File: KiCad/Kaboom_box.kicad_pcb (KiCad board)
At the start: 2 copper layers, 351.5 x 141.5 mm, 206 parts, among them J101 2mm_clamp, J102 2mm_clamp, J103 2mm_clamp, J104 2mm_clamp, J105 2mm_clamp, J106 2mm_clamp, J107 2mm_clamp, J108 2mm_clamp, J109 2mm_clamp, J110 2mm_clamp, J111 2mm_clamp, J112 2mm_clamp, J113 2mm_clamp, J114 2mm_clamp, J115 2mm_clamp, J116 2mm_clamp, J117 2mm_clamp, J118 2mm_clamp, J119 2mm_clamp, J120 2mm_clamp, J121 2mm_clamp, J122 2mm_clamp, J123 2mm_clamp, J124 2mm_clamp, J125 2mm_clamp, J126 2mm_clamp, J127 2mm_clamp, J128 2mm_clamp, J129 2mm_clamp, J130 2mm_clamp, J131 2mm_clamp, J132 2mm_clamp, J133 2mm_clamp, J134 2mm_clamp, J135 2mm_clamp, J136 2mm_clamp, J137 2mm_clamp, J138 2mm_clamp, J139 2mm_clamp, J140 2mm_clamp, J141 2mm_clamp, J142 2mm_clamp, J143 2mm_clamp, J144 2mm_clamp, J145 2mm_clamp, J146 2mm_clamp, J147 2mm_clamp, J148 2mm_clamp, J149 2mm_clamp, J150 2mm_clamp, J151 2mm_clamp, J152 2mm_clamp, J153 2mm_clamp, J154 2mm_clamp, J155 2mm_clamp, J156 2mm_clamp, J157 2mm_clamp, J158 2mm_clamp, J159 2mm_clamp, J160 2mm_clamp, J161 2mm_clamp, J162 Screw_Terminal_01x02, P101 HDR-IDC-2_54-2X5P, P102 HDR-IDC-2_54-2X5P, P103 HDR-IDC-2_54-2X5P, P104 HDR-IDC-2_54-2X5P, P105 HDR-IDC-2_54-2X5P, P106 HDR-IDC-2_54-2X5P, U101 SS54_C22452, U102 EC12E1220813, U103 RaspberryPi_Pico, U104 TS-1187A-B-A-B, U105 TS-1187A-B-A-B, U106 AO3400A, U107 WS2812E-MINI-X1, U108 WS2812E-MINI-X1, U109 WS2812E-MINI-X1, U110 WS2812E-MINI-X1, U111 WS2812E-MINI-X1, U112 WS2812E-MINI-X1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

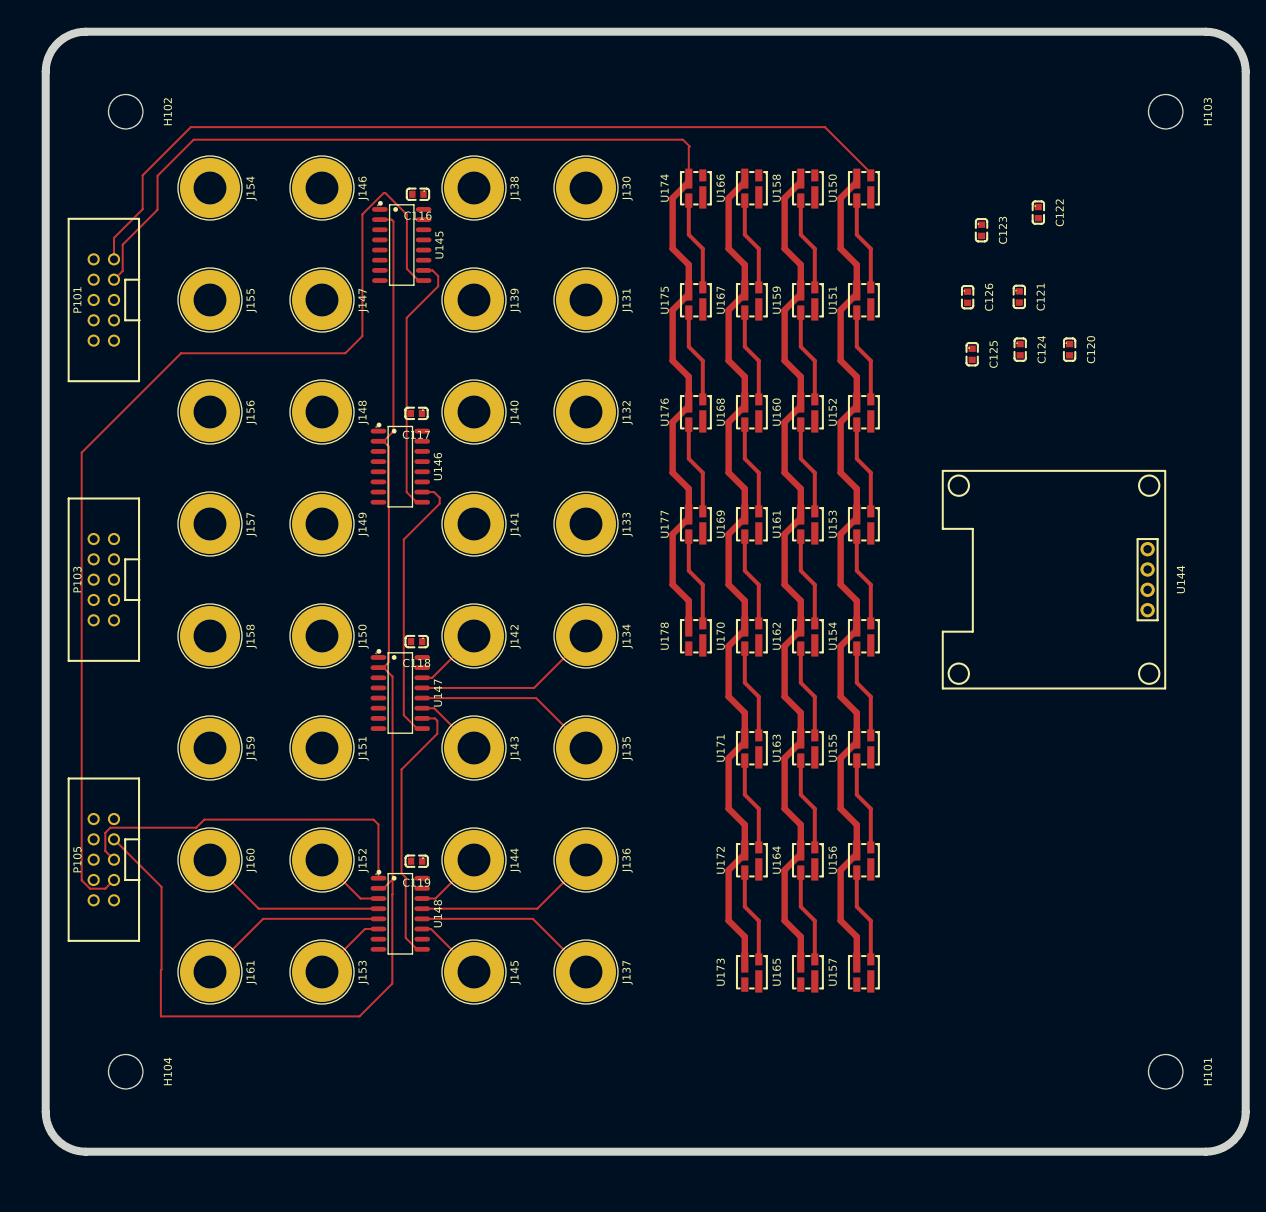
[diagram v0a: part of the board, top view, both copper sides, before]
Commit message: Update to TOP pcb - 2mm holes placement and routing
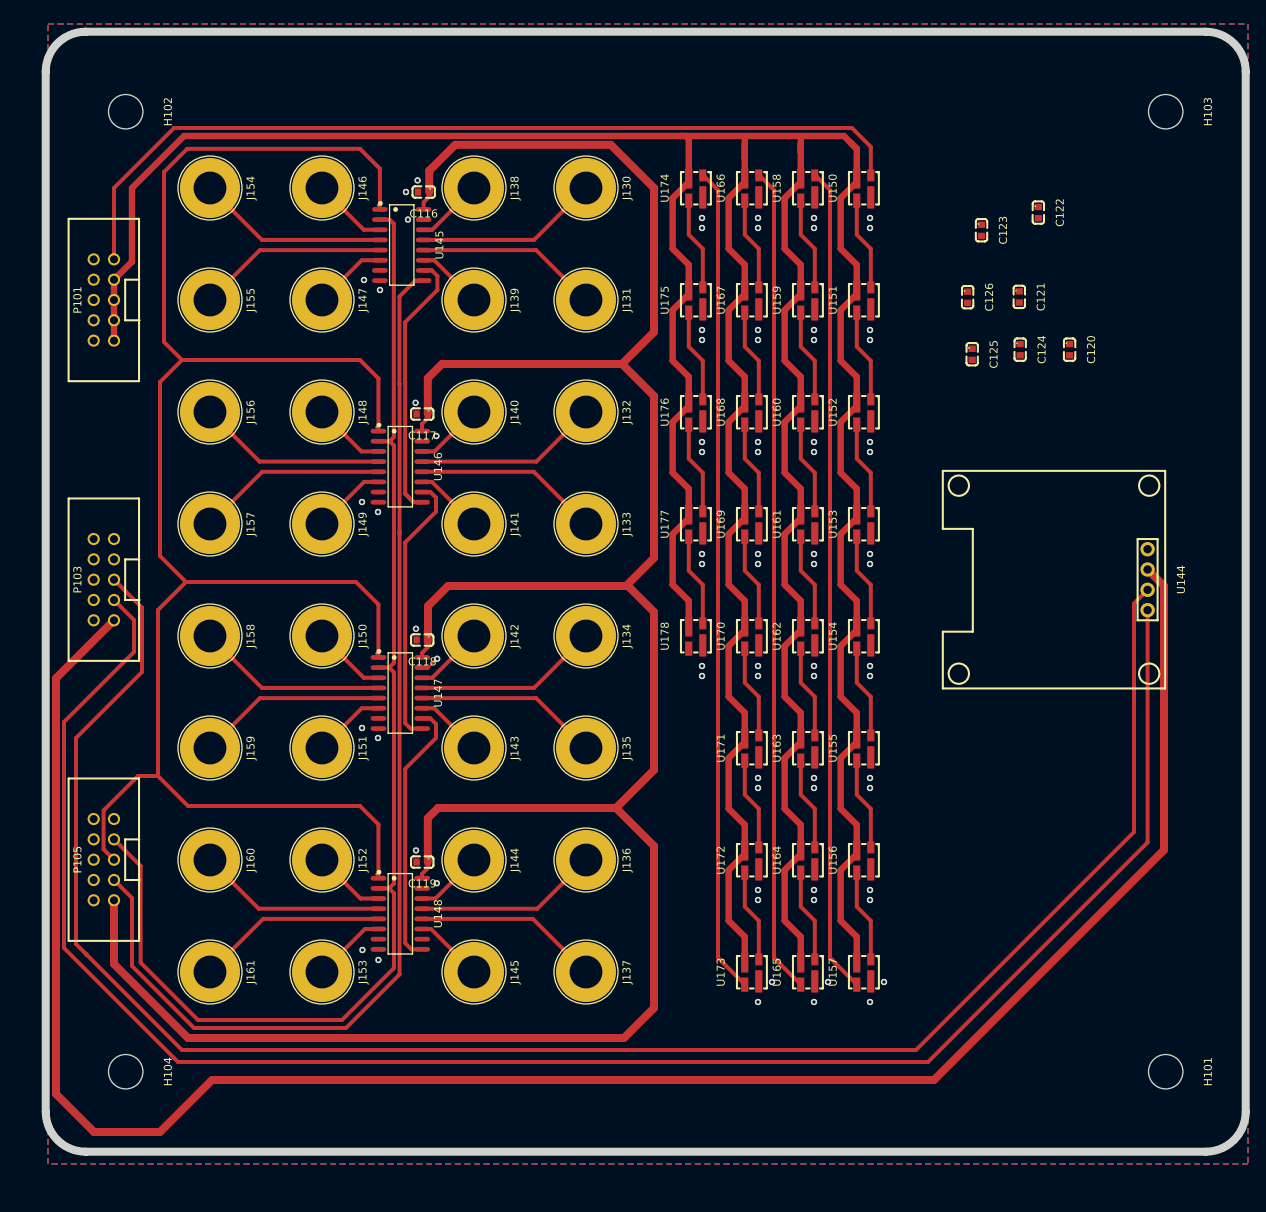
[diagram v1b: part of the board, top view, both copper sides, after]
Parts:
- moved C116 0.77 mm to (298.7, 81.5)
- moved C117 0.73 mm to (298.5, 109.2)
- moved C118 0.72 mm to (298.5, 137.5)
- moved C119 0.70 mm to (298.5, 165.2)
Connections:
- net Net-(J134-Pin_1) renamed /Top/Shift_Parallel_to_Serial/J134
- net Net-(J135-Pin_1) renamed /Top/Shift_Parallel_to_Serial/J135
- net Net-(J136-Pin_1) renamed /Top/Shift_Parallel_to_Serial/J136
- net Net-(J137-Pin_1) renamed /Top/Shift_Parallel_to_Serial/J137
- net Net-(J142-Pin_1) renamed /Top/Shift_Parallel_to_Serial/J142
- net Net-(J143-Pin_1) renamed /Top/Shift_Parallel_to_Serial/J143
- net Net-(J144-Pin_1) renamed /Top/Shift_Parallel_to_Serial/J144
- net Net-(J145-Pin_1) renamed /Top/Shift_Parallel_to_Serial/J145
- net Net-(J152-Pin_1) renamed /Top/Shift_Parallel_to_Serial/J152
- net Net-(J153-Pin_1) renamed /Top/Shift_Parallel_to_Serial/J153
- net Net-(J160-Pin_1) renamed /Top/Shift_Parallel_to_Serial/J160
- net Net-(J161-Pin_1) renamed /Top/Shift_Parallel_to_Serial/J161
- J130 pad 1: Net-(J130-Pin_1) -> /Top/Shift_Parallel_to_Serial/J130
- J131 pad 1: Net-(J131-Pin_1) -> /Top/Shift_Parallel_to_Serial/J131
- J132 pad 1: Net-(J132-Pin_1) -> /Top/Shift_Parallel_to_Serial/J132
- J133 pad 1: Net-(J133-Pin_1) -> /Top/Shift_Parallel_to_Serial/J133
- J138 pad 1: Net-(J138-Pin_1) -> /Top/Shift_Parallel_to_Serial/J138
- J139 pad 1: Net-(J139-Pin_1) -> /Top/Shift_Parallel_to_Serial/J139
- J140 pad 1: Net-(J140-Pin_1) -> /Top/Shift_Parallel_to_Serial/J140
- J141 pad 1: Net-(J141-Pin_1) -> /Top/Shift_Parallel_to_Serial/J141
- J146 pad 1: unconnected-(J146-Pin_1-Pad1) -> /Top/Shift_Parallel_to_Serial/J146
- J147 pad 1: unconnected-(J147-Pin_1-Pad1) -> /Top/Shift_Parallel_to_Serial/J147
- J148 pad 1: unconnected-(J148-Pin_1-Pad1) -> /Top/Shift_Parallel_to_Serial/J148
- J149 pad 1: unconnected-(J149-Pin_1-Pad1) -> /Top/Shift_Parallel_to_Serial/J149
- J150 pad 1: unconnected-(J150-Pin_1-Pad1) -> /Top/Shift_Parallel_to_Serial/J150
- J151 pad 1: unconnected-(J151-Pin_1-Pad1) -> /Top/Shift_Parallel_to_Serial/J151
- J154 pad 1: unconnected-(J154-Pin_1-Pad1) -> /Top/Shift_Parallel_to_Serial/J154
- J155 pad 1: unconnected-(J155-Pin_1-Pad1) -> /Top/Shift_Parallel_to_Serial/J155
- J156 pad 1: unconnected-(J156-Pin_1-Pad1) -> /Top/Shift_Parallel_to_Serial/J156
- J157 pad 1: unconnected-(J157-Pin_1-Pad1) -> /Top/Shift_Parallel_to_Serial/J157
- J158 pad 1: unconnected-(J158-Pin_1-Pad1) -> /Top/Shift_Parallel_to_Serial/J158
- J159 pad 1: unconnected-(J159-Pin_1-Pad1) -> /Top/Shift_Parallel_to_Serial/J159
- U145 pad 11: unconnected-(U145-D0-Pad11) -> /Top/Shift_Parallel_to_Serial/J139
- U145 pad 12: Net-(J139-Pin_1) -> /Top/Shift_Parallel_to_Serial/J131
- U145 pad 13: unconnected-(U145-D2-Pad13) -> /Top/Shift_Parallel_to_Serial/J130
- U145 pad 14: Net-(J131-Pin_1) -> /Top/Shift_Parallel_to_Serial/J138
- U145 pad 3: Net-(J130-Pin_1) -> /Top/Shift_Parallel_to_Serial/J146
- U145 pad 4: unconnected-(U145-D5-Pad4) -> /Top/Shift_Parallel_to_Serial/J154
- U145 pad 5: Net-(J138-Pin_1) -> /Top/Shift_Parallel_to_Serial/J155
- U145 pad 6: unconnected-(U145-D7-Pad6) -> /Top/Shift_Parallel_to_Serial/J147
- U146 pad 11: unconnected-(U146-D0-Pad11) -> /Top/Shift_Parallel_to_Serial/J141
- U146 pad 12: Net-(J141-Pin_1) -> /Top/Shift_Parallel_to_Serial/J133
- U146 pad 13: unconnected-(U146-D2-Pad13) -> /Top/Shift_Parallel_to_Serial/J132
- U146 pad 14: Net-(J133-Pin_1) -> /Top/Shift_Parallel_to_Serial/J140
- U146 pad 3: Net-(J132-Pin_1) -> /Top/Shift_Parallel_to_Serial/J148
- U146 pad 4: unconnected-(U146-D5-Pad4) -> /Top/Shift_Parallel_to_Serial/J156
- U146 pad 5: Net-(J140-Pin_1) -> /Top/Shift_Parallel_to_Serial/J157
- U146 pad 6: unconnected-(U146-D7-Pad6) -> /Top/Shift_Parallel_to_Serial/J149
- U147 pad 3: unconnected-(U147-D4-Pad3) -> /Top/Shift_Parallel_to_Serial/J150
- U147 pad 4: unconnected-(U147-D5-Pad4) -> /Top/Shift_Parallel_to_Serial/J158
- U147 pad 5: unconnected-(U147-D6-Pad5) -> /Top/Shift_Parallel_to_Serial/J159
- U147 pad 6: unconnected-(U147-D7-Pad6) -> /Top/Shift_Parallel_to_Serial/J151
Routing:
- net /Top/+3.3V: track 0.00 -> 580.2 mm
- net /I2C_SCL_LID: track 0.00 -> 230.8 mm
- net /I2C1_SDA_LID: track 0.00 -> 229.9 mm
- net /SPI0_CSn_LID: track 45.6 -> 230.7 mm
- net Net-(U173-DO): track 0.00 -> 103.4 mm
- net Net-(U165-DO): track 0.00 -> 103.4 mm
- net Net-(U157-DO): track 0.00 -> 103.4 mm
- net /Top/VDD: track 498.9 -> 549.7 mm
- net /Top/Shift_Parallel_to_Serial/J154: track 0.00 -> 23.9 mm
- net /Top/Shift_Parallel_to_Serial/J155: track 0.00 -> 23.8 mm
- net /Top/Shift_Parallel_to_Serial/J157: track 0.00 -> 23.8 mm
- net /Top/Shift_Parallel_to_Serial/J158: track 0.00 -> 23.7 mm
- net /Top/Shift_Parallel_to_Serial/J159: track 0.00 -> 23.6 mm
- net /Top/Shift_Parallel_to_Serial/J156: track 0.00 -> 23.6 mm
- net /Top/Shift_Parallel_to_Serial/J133: track 0.00 -> 23.2 mm
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- added copper zone on B.Cu, net /Top/GND
- added copper zone on F.Cu, net /Top/GND

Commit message: WIP on Bottom
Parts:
- moved R104 18.9 mm to (98.5, 181.2)
- moved R103 4.41 mm to (105.8, 182.3)
- moved R111 3.43 mm to (98.5, 153.2), turned to 180 degrees
- moved R110 3.15 mm to (98.5, 155.7), turned to 180 degrees
- moved R102 3.03 mm to (105.8, 179.8)
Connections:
- U103 pad 16: unconnected-(U103-GPIO12-Pad16) -> /Bottom/+3.3V
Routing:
- net /Bottom/VDD: track 525.4 -> 870.2 mm
- net /I2C_SCL_BOT: track 4.90 -> 265.3 mm, vias 0 -> 2
- net /I2C1_SDA_BOT: track 4.89 -> 261.9 mm, vias 0 -> 2
- net /Bottom/LED_DATA_OUT: track 0.00 -> 254.9 mm
- net /Bottom/+3.3V: track 270.2 -> 443.5 mm
- net Net-(J101-Pin_1): track 0.00 -> 117.4 mm
- net Net-(U130-DO): track 0.00 -> 103.3 mm
- net Net-(U122-DO): track 0.00 -> 103.3 mm
- net Net-(U114-DO): track 0.00 -> 103.3 mm
- net Net-(J104-Pin_1): track 0.00 -> 96.8 mm
- net /Bottom/SPI1_CSn: track 49.9 -> 142.2 mm, vias 3 -> 11
- net /Bottom/SPI1_RST: track 48.9 -> 140.8 mm, vias 4 -> 6
- net Net-(J107-Pin_1): track 0.00 -> 82.7 mm
- net /Bottom/SPI1_TX: track 67.7 -> 143.8 mm
- net /Bottom/SPI1_SCK: track 84.8 -> 157.7 mm
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
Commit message: Layout wip
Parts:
- J162: moved to B.Cu
- moved D102 44.1 mm to (137.2, 174.7)
- moved U149 40.6 mm to (138.8, 181.6), turned to 180 degrees
- moved R120 40.1 mm to (134.8, 181.7), turned to -90 degrees
- moved J162 39.5 mm to (139.9, 177.7), turned to 180 degrees
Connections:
- net /Bottom/SPI1_RST renamed /Bottom/SPI0_RST
- R104 pad 2: /SPI0_RX_BOT -> /Bottom/SPI0_RX
- R105 pad 2: /SPI0_CSn_BOT -> /Bottom/SPI0_CSn
- R110 pad 2: /Bottom/SPI1_RX -> /SPI0_RX_BOT
- R111 pad 2: /Bottom/SPI1_CSn -> /SPI0_CSn_BOT
- U103 pad 1: /SPI0_RX_BOT -> /Bottom/SPI0_RX
- U103 pad 11: /Bottom/SPI1_RX -> /SPI0_RX_BOT
- U103 pad 12: /Bottom/SPI1_CSn -> /SPI0_CSn_BOT
- U103 pad 14: /Bottom/SPI1_SCK -> /SPI0_SCK_BOT
- U103 pad 15: /Bottom/SPI1_TX -> /SPI0_TX_BOT
- U103 pad 2: /SPI0_CSn_BOT -> /Bottom/SPI0_CSn
- U103 pad 4: /SPI0_SCK_BOT -> /Bottom/SPI0_SCK
- U103 pad 5: /SPI0_TX_BOT -> /Bottom/SPI0_TX
- U136 pad 11: /Bottom/SPI1_SCK -> /Bottom/SPI0_SCK
- U136 pad 12: /Bottom/SPI1_SCK -> /Bottom/SPI0_SCK
- U136 pad 13: /Bottom/SPI1_CSn -> /Bottom/SPI0_CSn
- U136 pad 14: /Bottom/SPI1_TX -> /Bottom/SPI0_TX
- U137 pad 11: /Bottom/SPI1_SCK -> /Bottom/SPI0_SCK
- U137 pad 12: /Bottom/SPI1_SCK -> /Bottom/SPI0_SCK
- U137 pad 13: /Bottom/SPI1_CSn -> /Bottom/SPI0_CSn
- U138 pad 11: /Bottom/SPI1_SCK -> /Bottom/SPI0_SCK
- U138 pad 12: /Bottom/SPI1_SCK -> /Bottom/SPI0_SCK
- U138 pad 13: /Bottom/SPI1_CSn -> /Bottom/SPI0_CSn
- U139 pad 11: /Bottom/SPI1_SCK -> /Bottom/SPI0_SCK
- U139 pad 12: /Bottom/SPI1_SCK -> /Bottom/SPI0_SCK
- U139 pad 13: /Bottom/SPI1_CSn -> /Bottom/SPI0_CSn
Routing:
- net /SPI0_SCK_BOT: track 0.00 -> 198.1 mm
- net /SPI0_TX_BOT: track 7.59 -> 197.2 mm, vias 2 -> 0
- net /SPI0_CSn_BOT: track 4.92 -> 194.4 mm
- net /SPI0_RX_BOT: track 6.73 -> 186.7 mm
- net /Bottom/SPI1_SCK: track 157.7 -> 0.00 mm
- net /Bottom/SPI1_TX: track 143.8 -> 0.00 mm
- net /Bottom/SPI1_CSn: track 142.2 -> 0.00 mm, vias 11 -> 0
- net /Bottom/SPI0_SCK: track 0.00 -> 124.7 mm
- net /Bottom/SPI0_TX: track 0.00 -> 114.9 mm
- net /Bottom/SPI0_CSn: track 0.00 -> 109.8 mm, vias 0 -> 11
- net /Bottom/RUMBLE: track 0.00 -> 92.4 mm
- net /Bottom/SPI0_RST: track 140.8 -> 202.7 mm, vias 6 -> 8
- net /Bottom/+3.3V: track 443.5 -> 430.0 mm
- net Net-(D102-A): track 0.00 -> 8.04 mm
- net /Bottom/SPI0_RX: track 0.00 -> 6.73 mm
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
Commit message: Ready for review
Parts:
- removed the H101 at (391.5, 191.5)
- removed the H102 at (261.5, 71.5)
- removed the H103 at (391.5, 71.5)
- removed the H104 at (261.5, 191.5)
- removed J159, J160, J161: 2mm_clamp, Kaboom_box:2mm testlead, screw-clamp
- added B101: Board, PCM_kikit:Board, F.Cu at (57.2, 60.0)
- added B102: Board, PCM_kikit:Board, F.Cu at (258.3, 61.5)
- added H105: MountingHole, MountingHole:MountingHole_4.3mm_M4, F.Cu at (391.5, 71.5)
- added H106: MountingHole, MountingHole:MountingHole_4.3mm_M4, F.Cu at (261.5, 71.5)
- added H107: MountingHole, MountingHole:MountingHole_4.3mm_M4, F.Cu at (391.5, 191.5)
- added H108: MountingHole, MountingHole:MountingHole_4.3mm_M4, F.Cu at (261.5, 191.5)
- U103: footprint Module_RaspberryPi_Pico:RaspberryPi_Pico_Original_SMD_Castellated_HandSolder -> Module_RaspberryPi_Pico:RaspberryPi_Pico_Common_No_Keepout
- moved C123 76.5 mm to (344.0, 158.8), turned to 90 degrees
- moved C121 67.9 mm to (351.0, 158.8), turned to 90 degrees
- moved C125 64.6 mm to (336.8, 158.8), turned to 90 degrees
- moved C126 37.6 mm to (330.0, 102.8), turned to 90 degrees
- moved C122 36.7 mm to (344.0, 102.8), turned to 90 degrees
- moved C124 36.3 mm to (337.0, 102.8), turned to 90 degrees
- moved C120 28.5 mm to (351.0, 102.8), turned to 90 degrees
- moved R106 6.51 mm to (57.4, 106.0), turned to 0 degrees
- moved R107 6.44 mm to (57.3, 122.0), turned to 180 degrees
- moved C107 3.41 mm to (101.5, 102.5), turned to 90 degrees
- moved C106 3.38 mm to (109.0, 158.0), turned to 90 degrees
- moved C105 3.15 mm to (109.0, 102.5), turned to 90 degrees
- moved C101 3.05 mm to (123.2, 102.5), turned to 90 degrees
- moved C102 3.05 mm to (123.2, 158.2), turned to 90 degrees
- moved C103 3.05 mm to (116.2, 102.5), turned to 90 degrees
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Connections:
- C116 pad 1: /Top/+3.3V -> /Top/+3.3V_SHIFT
- C117 pad 1: /Top/+3.3V -> /Top/+3.3V_SHIFT
- C118 pad 1: /Top/+3.3V -> /Top/+3.3V_SHIFT
- C119 pad 1: /Top/+3.3V -> /Top/+3.3V_SHIFT
- P103 pad 1: /Top/+3.3V -> /Top/+3.3V_OLED
- P105 pad 1: /Top/+3.3V -> /Top/GND
- P105 pad 10: /Top/GND -> /Top/+3.3V_SHIFT
- P105 pad 2: /Top/GND -> /SPI0_TX_LID
- P105 pad 3: /SPI0_RX_LID -> /Top/GND
- P105 pad 4: /Top/GND -> /SPI0_SCK_LID
- P105 pad 5: /SPI0_CSn_LID -> /Top/GND
- P105 pad 6: /Top/GND -> /SPI0_CSn_LID
- P105 pad 7: /SPI0_SCK_LID -> /Top/GND
- P105 pad 8: /Top/GND -> /SPI0_RX_LID
- P105 pad 9: /SPI0_TX_LID -> /Top/GND
- P106 pad 1: /Bottom/+3.3V -> GND
- P106 pad 10: GND -> /Bottom/+3.3V
- P106 pad 2: GND -> /SPI0_TX_BOT
- P106 pad 3: /SPI0_RX_BOT -> GND
- P106 pad 4: GND -> /SPI0_SCK_BOT
- P106 pad 5: /SPI0_CSn_BOT -> GND
- P106 pad 6: GND -> /SPI0_CSn_BOT
- P106 pad 7: /SPI0_SCK_BOT -> GND
- P106 pad 8: GND -> /SPI0_RX_BOT
- P106 pad 9: /SPI0_TX_BOT -> GND
- U144 pad 2: /Top/+3.3V -> /Top/+3.3V_OLED
- U145 pad 16: /Top/+3.3V -> /Top/+3.3V_SHIFT
- U146 pad 16: /Top/+3.3V -> /Top/+3.3V_SHIFT
- U147 pad 16: /Top/+3.3V -> /Top/+3.3V_SHIFT
- U148 pad 16: /Top/+3.3V -> /Top/+3.3V_SHIFT
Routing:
- net /Top/+3.3V: track 582.9 -> 0.00 mm
- net /Top/+3.3V_SHIFT: track 0.00 -> 343.2 mm
- net /Bottom/VDD: track 876.9 -> 1162.2 mm
- net /Top/+3.3V_OLED: track 0.00 -> 253.4 mm
- net GND: track 6.05 -> 50.5 mm, vias 5 -> 179
- net /Top/Shift_Parallel_to_Serial/J161: track 23.8 -> 0.00 mm
- net /Top/Shift_Parallel_to_Serial/J159: track 23.6 -> 0.00 mm
- net /Top/Shift_Parallel_to_Serial/J160: track 23.6 -> 0.00 mm
- net (no net): track 15.6 -> 0.00 mm
- net /Bottom/+3.3V: track 430.0 -> 416.4 mm, vias 8 -> 9
- net Net-(LED102-A): track 0.00 -> 13.6 mm
- net /Bottom/LED_DATA_OUT: track 254.9 -> 246.5 mm
- net /SPI0_RX_LID: track 140.0 -> 146.5 mm
- net /I2C_SCL_BOT: track 264.8 -> 260.5 mm
- net /Bottom/DT: track 34.6 -> 38.4 mm
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- added copper zone on B.Cu, net GND
- added copper zone on F.Cu, net GND
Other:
- rule pad_to_mask_clearance: 0 -> 0.05
- board text added: "A"
- board text added: "B"
- board text added: "C"
- board text added: "D"
- board text added: "E"
- board text added: "F"
- board text added: "G"
- board text added: "H"
- board text added: "I"
- board text added: "J"
- board text added: "K"
- board text added: "L"
- board text added: "M"
- board text added: "N"
- board text added: "O"
- board text added: "P"
- board text added: "Q"
- board text added: "R"
- board text added: "S"
- board text added: "T"
- board text added: "U"
- board text added: "V"
- board text added: "W"
- board text added: "X"
- board text added: "Y"
- board text added: "Z"
- board text added: "Å"
- board text added: "Æ"
- board text added: "Ø"

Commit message: Updated to generate JLCPCB files
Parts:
- added C127: RVT0J102M0810, footprint:CAP-SMD_BD8.0-L8.3-W8.3-FD, F.Cu at (58.1, 150.3)
- added C128: RVT0J102M0810, footprint:CAP-SMD_BD8.0-L8.3-W8.3-FD, F.Cu at (360.1, 73.3)
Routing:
- net /Top/VDD: track 550.1 -> 581.1 mm
- net /Top/LED_DATA_IN: track 113.1 -> 123.7 mm
- net /Bottom/VDD: track 1162.2 -> 1162.8 mm
- net GND: vias 179 -> 187
- net /Top/GND: vias 191 -> 200

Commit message: PCB V1
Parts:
- U140, U141, U142: value MT-0-102-A101-M200-RS+PJ -> MT-0-103-F001-T000-RS+PJ
- moved C128 3.15 mm to (363.3, 73.2)
- moved C126 2.40 mm to (329.9, 100.3)
- moved C120 2.40 mm to (351.0, 100.3)
- moved C122 2.40 mm to (344.0, 100.3)
- moved C124 2.40 mm to (337.0, 100.3)
- moved C121 2.30 mm to (351.0, 156.4)
- moved C123 2.30 mm to (344.0, 156.4)
- moved C125 2.30 mm to (336.8, 156.4)
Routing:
- net /Top/VDD: track 581.1 -> 587.4 mm
- net /Top/LED_DATA_IN: track 123.7 -> 130.0 mm
- net /I2C_SCL_LID: track 231.8 -> 233.5 mm
- net /I2C1_SDA_LID: track 228.2 -> 229.6 mm
- net /Top/+3.3V_OLED: track 253.2 -> 254.4 mm
- net /Top/GND: vias 200 -> 209
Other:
- board text added: "Alfreds Kabooom Box"
- board text added: "If found: Please call Jakob 0045 28741982"
